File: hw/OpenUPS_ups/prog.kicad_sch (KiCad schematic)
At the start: 3 parts, among them J501 Conn_01x03

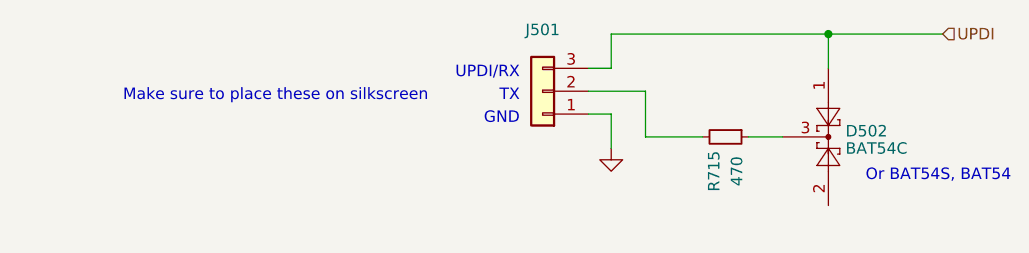
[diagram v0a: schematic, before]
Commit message: External I2C isolator
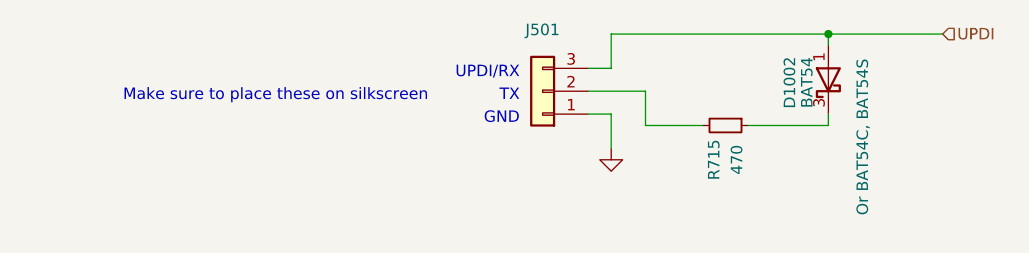
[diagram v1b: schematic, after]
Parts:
- removed D502: BAT54C, Package_TO_SOT_SMD:SOT-23, symbol Diode:BAT54C
- added D1002: BAT54, Package_TO_SOT_SMD:SOT-23, symbol Diode:BAT54W
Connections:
- net UPDI: now also D1002.1 (A)
- net at R715.1: now also D1002.3 (K)
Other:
- note removed: "Or BAT54S, BAT54"
- moved on the sheet: R715
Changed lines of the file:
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@@
   (junction (at 161.29 85.09) (diameter 0) (color 0 0 0 0)
+  )
+  (wire (pts (xy 161.29 93.98) (xy 161.29 95.25))
+    (stroke (width 0) (type default))
   )
   (wire (pts (xy 134.62 91.44) (xy 140.97 91.44))
     (stroke (width 0) (type default))
   )
-  (wire (pts (xy 140.97 96.52) (xy 147.32 96.52))
+  (wire (pts (xy 140.97 95.25) (xy 147.32 95.25))
     (stroke (width 0) (type default))
   )
   (wire (pts (xy 137.16 85.09) (xy 161.29 85.09))
+    (stroke (width 0) (type default))
+  )
+  (wire (pts (xy 161.29 95.25) (xy 152.4 95.25))
     (stroke (width 0) (type default))
   )
@@
     (stroke (width 0) (type default))
   )
-  (wire (pts (xy 140.97 91.44) (xy 140.97 96.52))
+  (wire (pts (xy 140.97 91.44) (xy 140.97 95.25))
     (stroke (width 0) (type default))
   )
-  (wire (pts (xy 161.29 85.09) (xy 161.29 88.9))
+  (wire (pts (xy 161.29 85.09) (xy 161.29 86.36))
     (stroke (width 0) (type default))
   )
   (wire (pts (xy 137.16 88.9) (xy 137.16 85.09))
     (stroke (width 0) (type default))
-  )
-  (wire (pts (xy 152.4 96.52) (xy 156.21 96.52))
-    (stroke (width 0) (type default))
-  )
-  (text "Or BAT54S, BAT54" (at 181.61 101.6 0)
-    (effects (font (size 1.27 1.27)) (justify right bottom))
   )
   (text "UPDI/RX" (at 127 90.17 0)
@@
     (effects (font (size 1.27 1.27)) (justify left))
   )
-  (symbol (lib_id "Device:R_Small") (at 149.86 96.52 270) (unit 1)
+  (symbol (lib_id "Device:R_Small") (at 149.86 95.25 270) (unit 1)
     (in_bom yes) (on_board yes) (dnp no)
-    (property "Reference" "R715" (at 148.59 100.33 0)
+    (property "Reference" "R715" (at 148.59 99.06 0)
       (effects (font (size 1.27 1.27)))
     )
-    (property "Value" "470" (at 151.13 100.33 0)
+    (property "Value" "470" (at 151.13 99.06 0)
       (effects (font (size 1.27 1.27)))
     )
-    (property "Footprint" "Resistor_SMD:R_0603_1608Metric" (at 149.86 96.52 0)
+    (property "Footprint" "Resistor_SMD:R_0603_1608Metric" (at 149.86 95.25 0)
       (effects (font (size 1.27 1.27)) hide)
     )
-    (property "Datasheet" "~" (at 149.86 96.52 0)
+    (property "Datasheet" "~" (at 149.86 95.25 0)
       (effects (font (size 1.27 1.27)) hide)
     )
@@
         (path "/f77faec3-eac4-47f3-a2de-ec4a039f4502/8ef22562-ae5a-4c6d-85ce-f0b1dd2b9eff"
           (reference "R515") (unit 1)
-        )
-      )
-    )
-  )
-  (symbol (lib_id "Diode:BAT54C") (at 161.29 96.52 270) (unit 1)
-    (in_bom yes) (on_board yes) (dnp no)
-    (property "Reference" "D502" (at 163.195 95.8763 90)
-      (effects (font (size 1.27 1.27)) (justify left))
-    )
-    (property "Value" "BAT54C" (at 163.195 97.7973 90)
-      (effects (font (size 1.27 1.27)) (justify left))
-    )
-    (property "Footprint" "Package_TO_SOT_SMD:SOT-23" (at 164.465 98.425 0)
-      (effects (font (size 1.27 1.27)) (justify left) hide)
-    )
-    (property "Datasheet" "http://www.diodes.com/_files/datasheets/ds11005.pdf" (at 161.29 94.488 0)
-      (effects (font (size 1.27 1.27)) hide)
-    )
-    (pin "1")
-    (pin "2")
-    (pin "3")
-    (instances
-      (project "OpenUPS_ups"
-        (path "/f77faec3-eac4-47f3-a2de-ec4a039f4502/8ef22562-ae5a-4c6d-85ce-f0b1dd2b9eff"
-          (reference "D502") (unit 1)
         )
       )
@@
         )
       )
+    )
+  )
+  (symbol (lib_id "Diode:BAT54W") (at 161.29 90.17 90) (unit 1)
+    (in_bom yes) (on_board yes) (dnp no)
+    (property "Reference" "D1002" (at 157.0101 90.4875 0)
+      (effects (font (size 1.27 1.27)))
+    )
+    (property "Value" "BAT54" (at 158.9311 90.4875 0)
+      (effects (font (size 1.27 1.27)))
+    )
+    (property "Footprint" "Package_TO_SOT_SMD:SOT-23" (at 165.735 90.17 0)
+      (effects (font (size 1.27 1.27)) hide)
+    )
+    (property "Datasheet" "https://assets.nexperia.com/documents/data-sheet/BAT54W_SER.pdf" (at 161.29 90.17 0)
+      (effects (font (size 1.27 1.27)) hide)
+    )
+    (property "Comment" "Or BAT54C, BAT54S" (at 165.1 96.52 0)
+      (effects (font (size 1.27 1.27)))
+    )
+    (pin "1")
+    (pin "2")
+    (pin "3")
+    (instances
+      (project "OpenUPS_ups"
+        (path "/f77faec3-eac4-47f3-a2de-ec4a039f4502/8df8d962-7936-4f05-9ed7-4d48f457f001"
+          (reference "D1002") (unit 1)
+        )
+        (path "/f77faec3-eac4-47f3-a2de-ec4a039f4502/8ef22562-ae5a-4c6d-85ce-f0b1dd2b9eff"
+          (reference "D501") (unit 1)
+        )
+      )

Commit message: Issue #24 5th generation charger (may need some tuning)
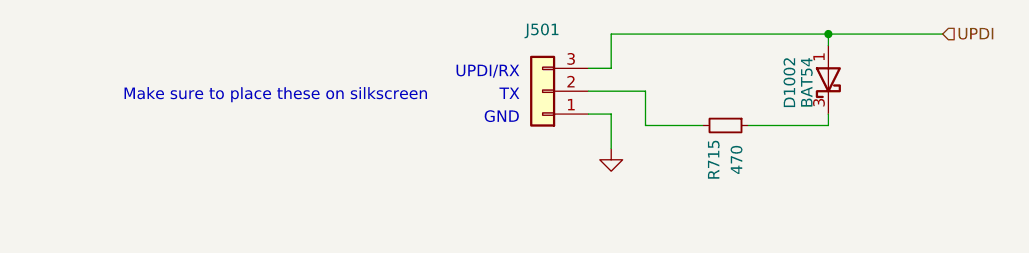
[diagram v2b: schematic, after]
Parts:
- D1002: Alt (none) -> BAT54C, BAT54S; Comment Or BAT54C, BAT54S -> (none)
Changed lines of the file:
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@@
       (effects (font (size 1.27 1.27)) hide)
     )
-    (property "Comment" "Or BAT54C, BAT54S" (at 165.1 96.52 0)
-      (effects (font (size 1.27 1.27)))
+    (property "Alt" "BAT54C, BAT54S" (at 165.1 96.52 0)
+      (effects (font (size 1.27 1.27)) hide)
     )
     (pin "1")
